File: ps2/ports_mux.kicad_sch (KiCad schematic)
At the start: 24 parts, among them Q1 BC547B, Q2 BC547B, Q3 BC547B, Q4 BC547B, U1 74HC74, U3 74HC32, U5 74HC32, U6 74HC02

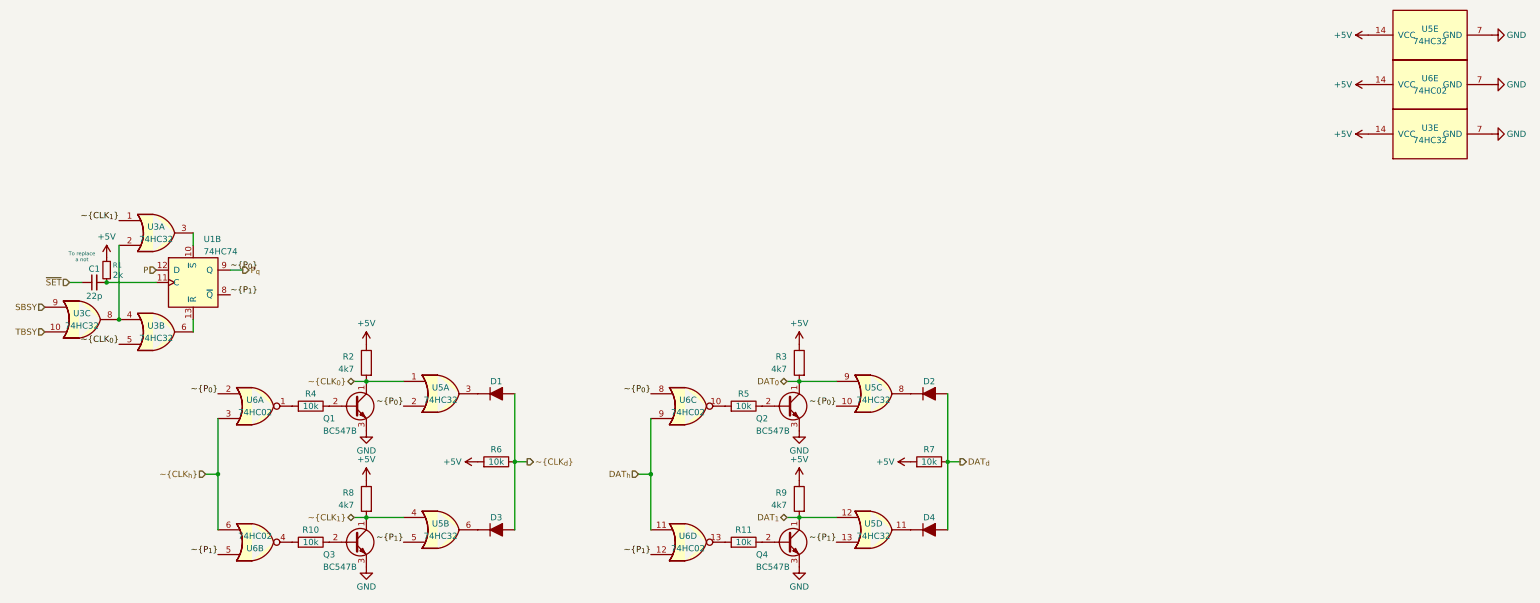
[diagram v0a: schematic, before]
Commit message: [ps2]:	made pcb design of the new latest schematic
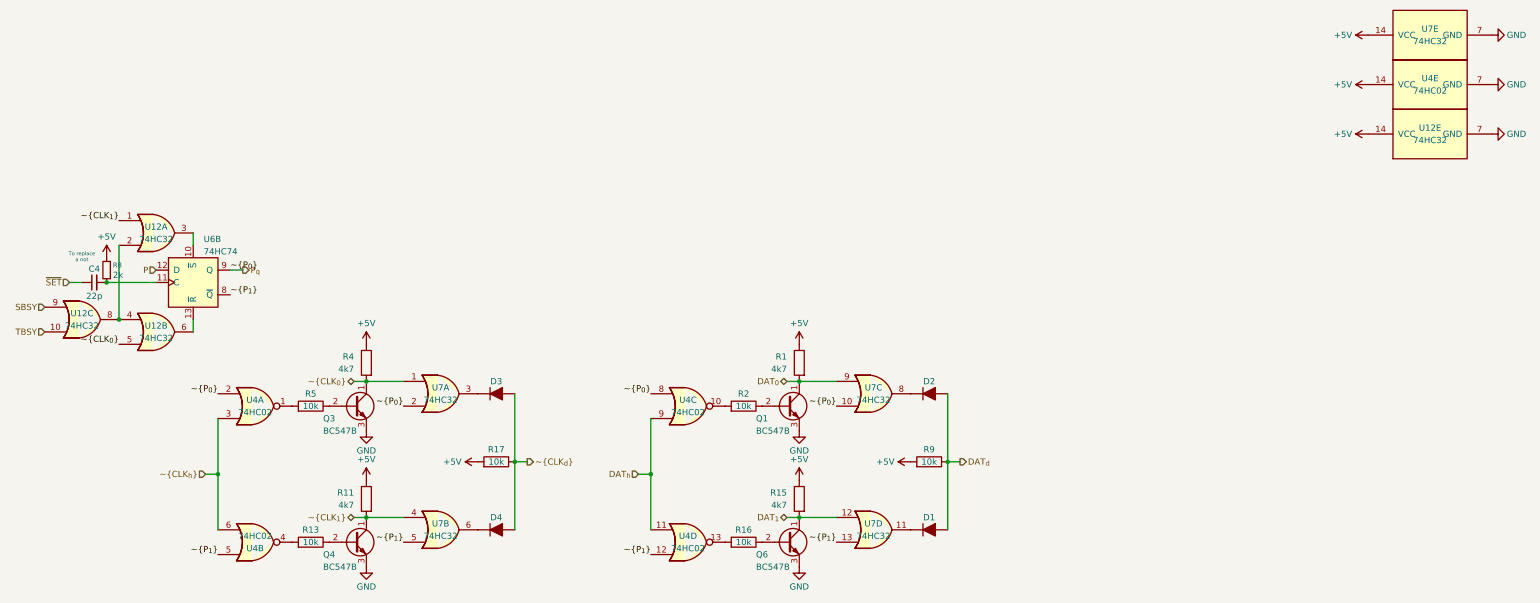
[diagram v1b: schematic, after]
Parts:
- renumbered C1 to C4, D4 to D1, D1 to D3, D3 to D4, Q2 to Q1, Q1 to Q3, Q3 to Q4, Q4 to Q6, R3 to R1, R8 to R11, R10 to R13, R9 to R15, R11 to R16, R6 to R17, R5 to R2, R2 to R4, R4 to R5, R1 to R8, R7 to R9, U3 to U12, U6 to U4, U1 to U6, U5 to U7
